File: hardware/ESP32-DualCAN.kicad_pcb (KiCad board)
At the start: 2 copper layers, 38.8 x 19.6 mm, 33 parts, among them J1 Molex 70553 6p, J2 Conn_01x10_Socket, J3 Conn_01x10_Socket, J4 holes, J5 pads, J6 holes, J7 pads, U1 LV2862Y, U3 TCAN1044AV, U4 TCAN1044AV, U5 ESP32-C6-Zero

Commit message: silk, pcba
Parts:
- added ?: , clipboard:03e50bc4-a574-419f-91ac-ebb8b02e042c, F.Cu at (160.2, 89.9)
- moved ? 0.38 mm to (159.1, 85.5)
- moved D6 0.20 mm to (156.4, 91.7)
- moved R9 0.05 mm to (158.3, 86.8)
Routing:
- net GND: track 80.9 -> 84.0 mm

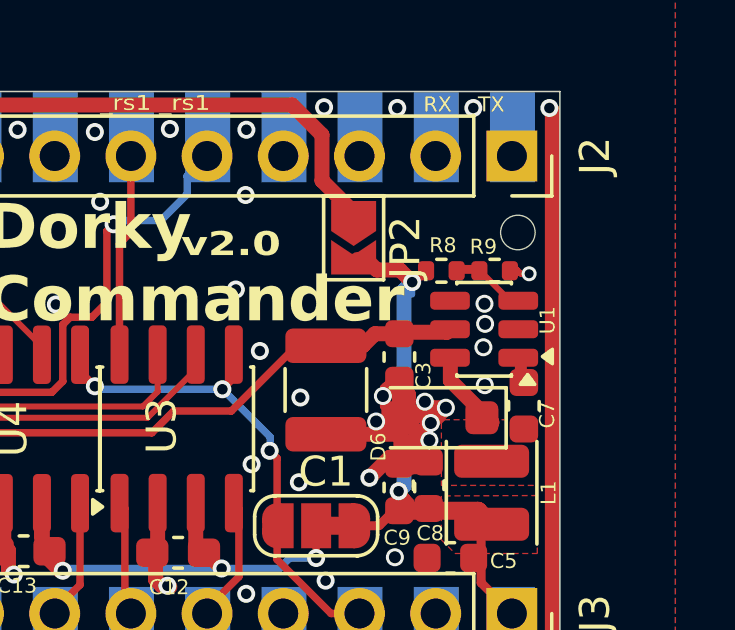
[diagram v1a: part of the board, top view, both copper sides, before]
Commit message: MLMR16006Y needs pull up on enable pin
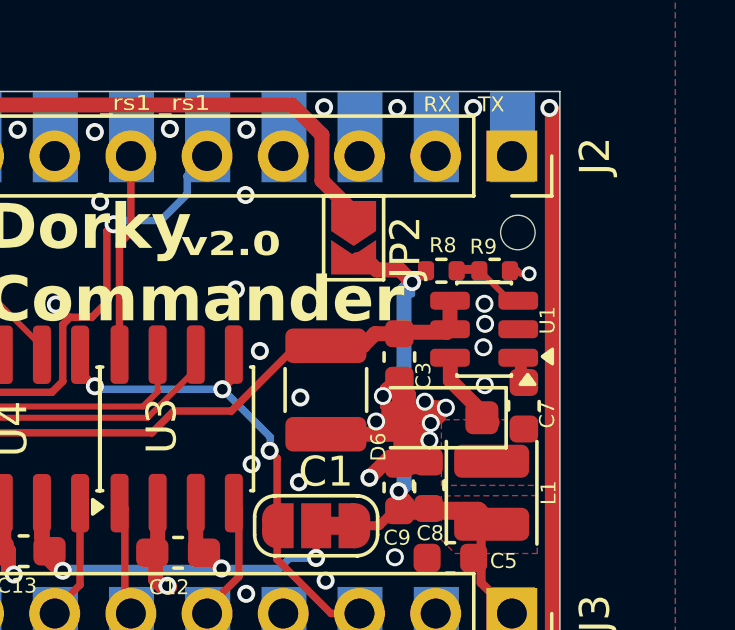
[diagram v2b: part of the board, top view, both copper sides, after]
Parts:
- U1: value LV2862Y -> MLMR16006Y
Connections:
- U1 pad 4: unconnected-(U1-EN-Pad4) -> /BATT_Diode
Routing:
- net /BATT_Diode: track 22.5 -> 23.5 mm
